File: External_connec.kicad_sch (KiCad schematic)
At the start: 12 parts, among them CN1 JST_Battery, J10 Conn_01x16_Socket, J2 A - B, J3 H - L, J4 TYPE-C-31-M12_13, J5 EXT_LOAD, J6 R4_TX, J7 R4_RX, J9 Conn_01x16_Socket

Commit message: Corrected schematic to PCB export error and warings and IP5306 and SD card section
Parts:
- CN1: footprint ESP32-S3_Dev_Board:CONN-SMD_2P-P1.00_SM02B-SRSS-TB-LF-SN -> ESP32-S3_Dev_Board:JST_2mm; LCSC Part C160402 -> C295747; PN SM02B-SRSS-TB (LF)(SN) -> S2B-PH-SM4-TB(LF)(SN)
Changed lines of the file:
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@@
       (effects (font (size 1.27 1.27)) hide)
     )
-    (property "Footprint" "ESP32-S3_Dev_Board:CONN-SMD_2P-P1.00_SM02B-SRSS-TB-LF-SN" (at 251.46 93.345 0)
+    (property "Footprint" "ESP32-S3_Dev_Board:JST_2mm" (at 251.46 93.345 0)
       (effects (font (size 1.27 1.27)) hide)
     )
-    (property "Datasheet" "https://lcsc.com/product-detail/Others_JST-Sales-America__JST-Sales-America-SM02B-SRSS-TB-LF-SN_C160402.html" (at 251.46 95.885 0)
+    (property "Datasheet" "https://datasheet.lcsc.com/lcsc/2102031704_JST-Sales-America-S2B-PH-SM4-TB-LF-SN_C295747.pdf" (at 251.46 95.885 0)
       (effects (font (size 1.27 1.27)) hide)
     )
-    (property "LCSC Part" "C160402" (at 251.46 98.425 0)
+    (property "LCSC Part" "C295747" (at 251.46 98.425 0)
       (effects (font (size 1.27 1.27)) hide)
     )
-    (property "PN" "SM02B-SRSS-TB (LF)(SN)" (at 251.46 89.535 0)
+    (property "PN" "S2B-PH-SM4-TB(LF)(SN) " (at 251.46 89.535 0)
       (effects (font (size 1.27 1.27)) hide)
     )

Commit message: Made minor changes in connectors sheet
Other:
- moved on the sheet: J10, J9

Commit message: Added CAN Jumpers, changed jumper pitch to 1.27mm
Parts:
- added J11: CAN_TX, ESP32-S3_Dev_Board:PinHeader_1x02_P1.27mm_Vertical, symbol ESP32-S3_DB:Conn_01x02
- added J12: CAN_RX, ESP32-S3_Dev_Board:PinHeader_1x02_P1.27mm_Vertical, symbol ESP32-S3_DB:Conn_01x02
- J6, J7: footprint ESP32-S3_Dev_Board:PinHeader_1x02_P2.54mm_Vertical -> ESP32-S3_Dev_Board:PinHeader_1x02_P1.27mm_Vertical
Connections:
- net CAN_RX renamed CAN_RX/GPIO8
- net CAN_RX/GPIO8: now also J12.1 (Pin_1)
- net CAN_TX renamed CAN_TX/GPIO7
- net CAN_TX/GPIO7: now also J11.1 (Pin_1)
- net RS-485_RX renamed RS-485_RX/GPIO46
- net RS-485_TX renamed RS-485_TX/GPIO45
- new net CAN_TRANS_RXD: J12.2 (Pin_2)
- new net CAN_TRANS_TXD: J11.2 (Pin_2)
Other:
- moved on the sheet: CN1

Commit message: Changed GPIO headers to Arduino style
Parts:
- removed J10, J9: Conn_01x16_Socket, ESP32-S3_Dev_Board:PinHeader_2x08_P2.54mm_Vertical, symbol ESP32-S3_DB:Conn_01x16_Socket
- added J13, J16: Conn_01x08, ESP32-S3_Dev_Board:PinHeader_1x08_P2.54mm_Vertical, symbol ESP32-S3_DB:Conn_01x08
- added J14, J9: Conn_01x06, ESP32-S3_Dev_Board:PinHeader_1x06_P2.54mm_Vertical, symbol ESP32-S3_DB:Conn_01x06
- added J15: Conn_01x10, ESP32-S3_Dev_Board:PinHeader_1x10_P2.54mm_Vertical, symbol ESP32-S3_DB:Conn_01x10
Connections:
- net 3V3: now also J16.5 (Pin_5), J9.6 (Pin_6)
- net 5V: now also J16.4 (Pin_4)
- net CAN_RX/GPIO8: now also J13.7 (Pin_7)
- net CAN_TX/GPIO7: now also J13.8 (Pin_8)
- net GND: now also J15.7 (Pin_7), J16.2 (Pin_2), J16.3 (Pin_3)
- net GPIO1: now also J14.1 (Pin_1)
- net GPIO14: now also J15.2 (Pin_2)
- net GPIO15: now also J15.3 (Pin_3)
- net GPIO16: now also J15.4 (Pin_4)
- net GPIO17: now also J15.5 (Pin_5)
- net GPIO18: now also J15.6 (Pin_6)
- net GPIO2: now also J14.2 (Pin_2)
- net GPIO21: now also J13.1 (Pin_1)
- net GPIO3: now also J14.3 (Pin_3)
- net GPIO33: now also J13.2 (Pin_2)
- net GPIO34: now also J13.3 (Pin_3)
- net GPIO35: now also J13.4 (Pin_4)
- net GPIO36: now also J13.5 (Pin_5)
- net GPIO37: now also J13.6 (Pin_6)
- net GPIO38: now also J15.9 (Pin_9)
- net GPIO39: now also J15.10 (Pin_10)
- net GPIO4: now also J14.4 (Pin_4)
- net GPIO40: now also J9.3 (Pin_3)
- net GPIO41: now also J9.4 (Pin_4)
- net GPIO42/~{RE}_DE: now also J9.5 (Pin_5)
- net GPIO5: now also J14.5 (Pin_5)
- net GPIO6: now also J14.6 (Pin_6)
- net GPIO9: now also J15.1 (Pin_1)
- net RS-485_RX/GPIO46: now also J9.2 (Pin_2)
- net RS-485_TX/GPIO45: now also J9.1 (Pin_1)
- new net RESET: J16.6 (Pin_6)
- no-connect marks 6 -> 10
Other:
- note added: "ADC GPIOs"
- note added: "DIGITAL GPIOs"
- note added: "JUMPER FOR USING CAN"
- note added: "POWER GPIOs"
- moved on the sheet: CN1, D11, J11, J12, J2, J3, J4, J5, J6, J7, R6, R7

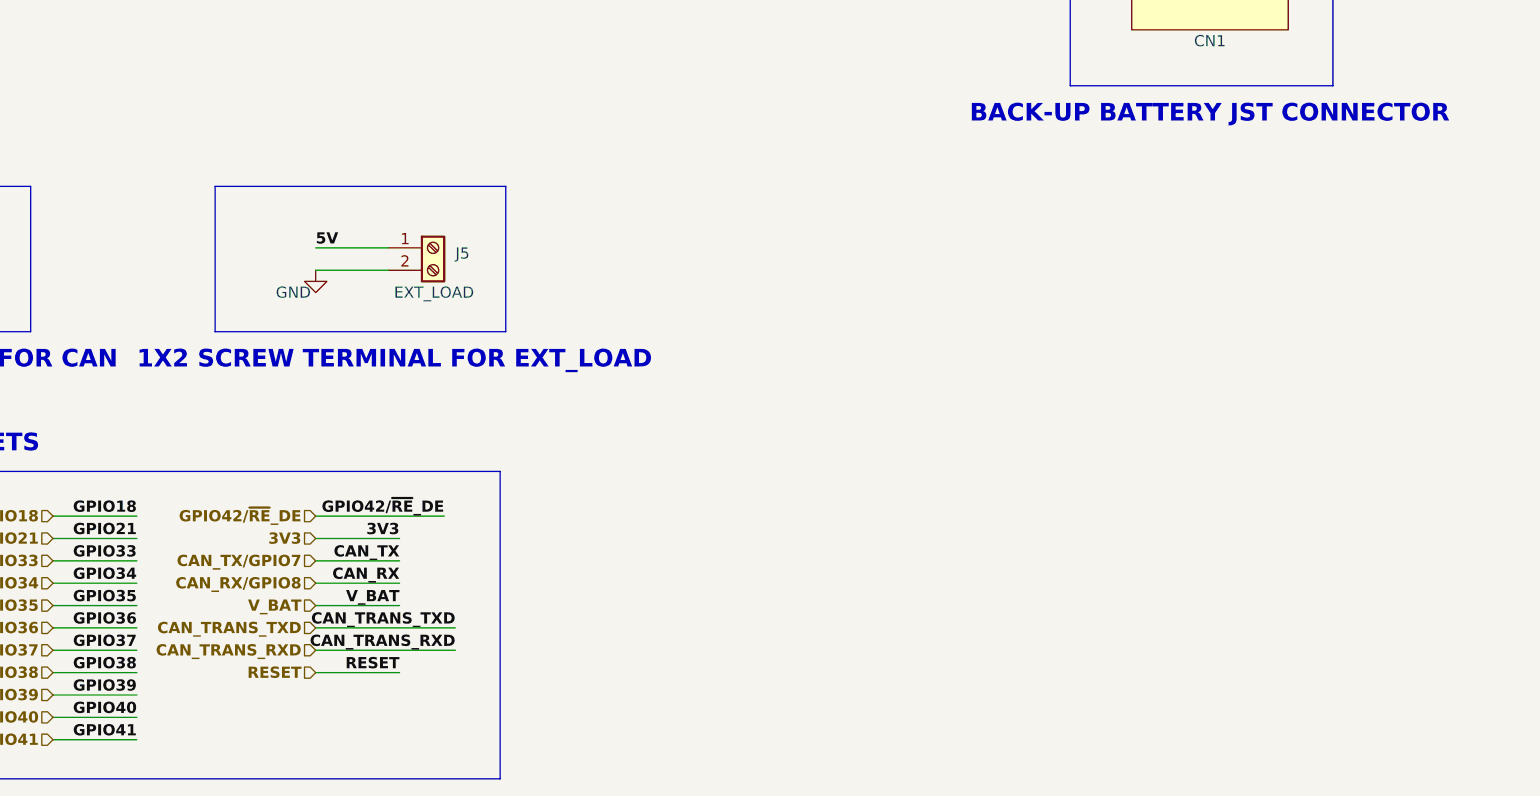
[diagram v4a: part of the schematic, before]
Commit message: Arranged IP5306, Added support for USB-To-RS485
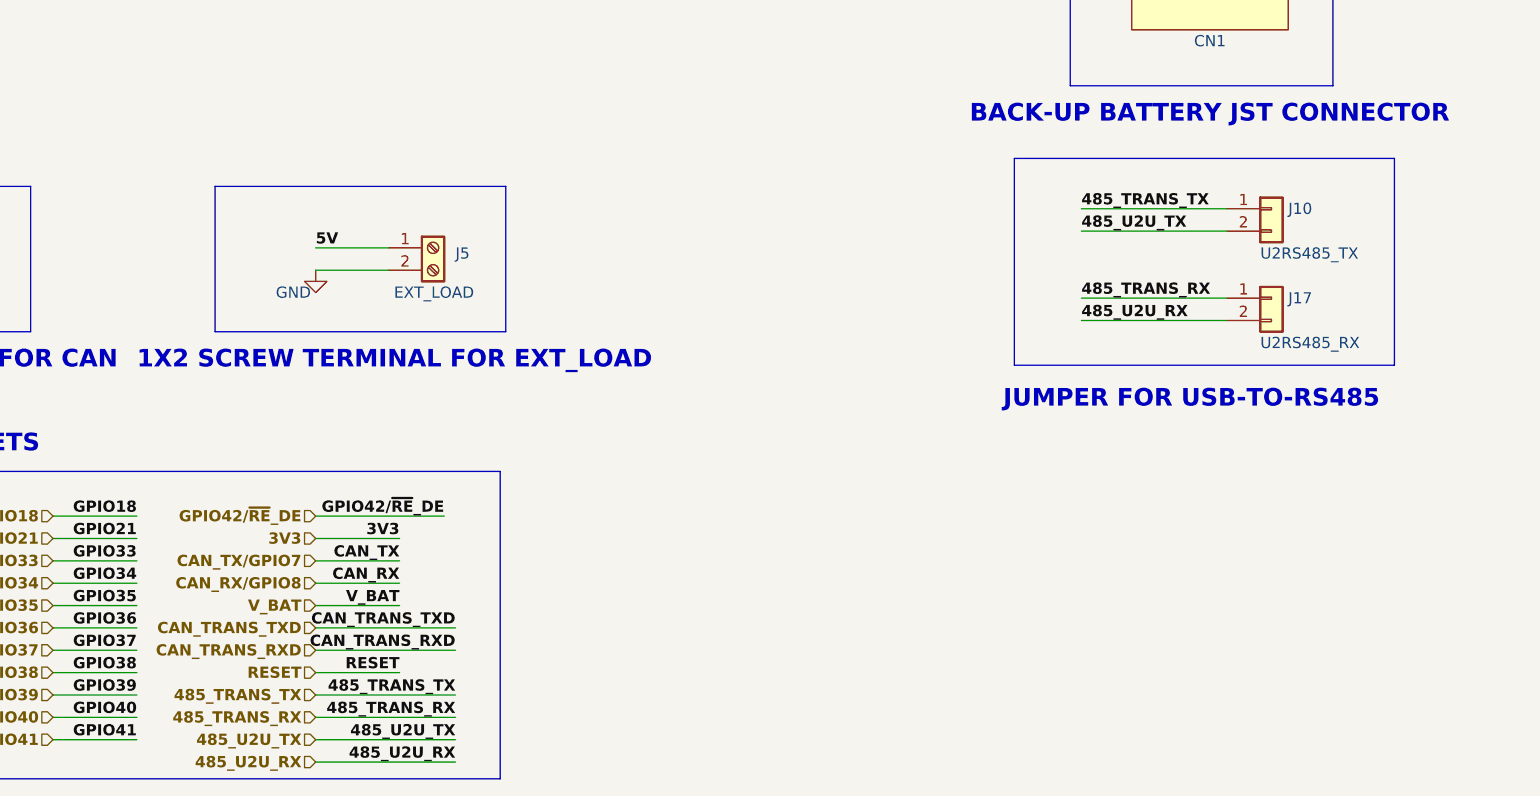
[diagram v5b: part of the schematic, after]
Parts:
- added J10: U2RS485_TX, ESP32-S3_Dev_Board:PinHeader_1x02_P1.27mm_Vertical, symbol ESP32-S3_DB:Conn_01x02
- added J17: U2RS485_RX, ESP32-S3_Dev_Board:PinHeader_1x02_P1.27mm_Vertical, symbol ESP32-S3_DB:Conn_01x02
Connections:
- new net 485_TRANS_RX: J17.1 (Pin_1)
- new net 485_TRANS_TX: J10.1 (Pin_1)
- new net 485_U2U_RX: J17.2 (Pin_2)
- new net 485_U2U_TX: J10.2 (Pin_2)
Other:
- note added: "JUMPER FOR USB-TO-RS485"

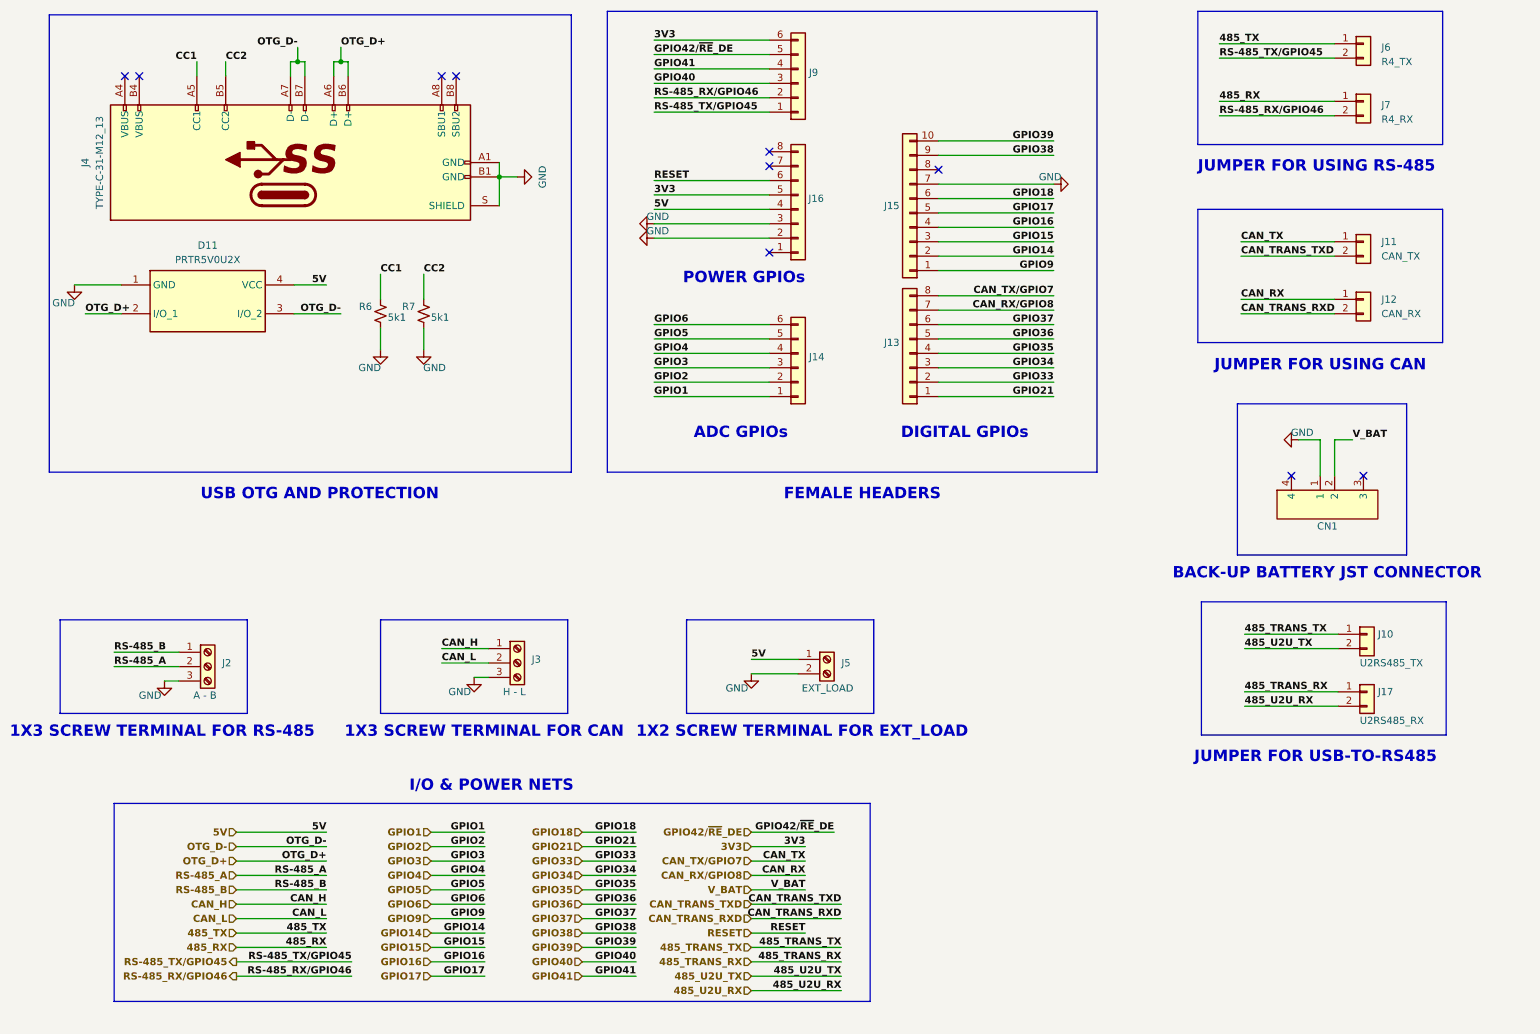
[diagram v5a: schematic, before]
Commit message: Added selection jumper sheet and USB-UART option for board
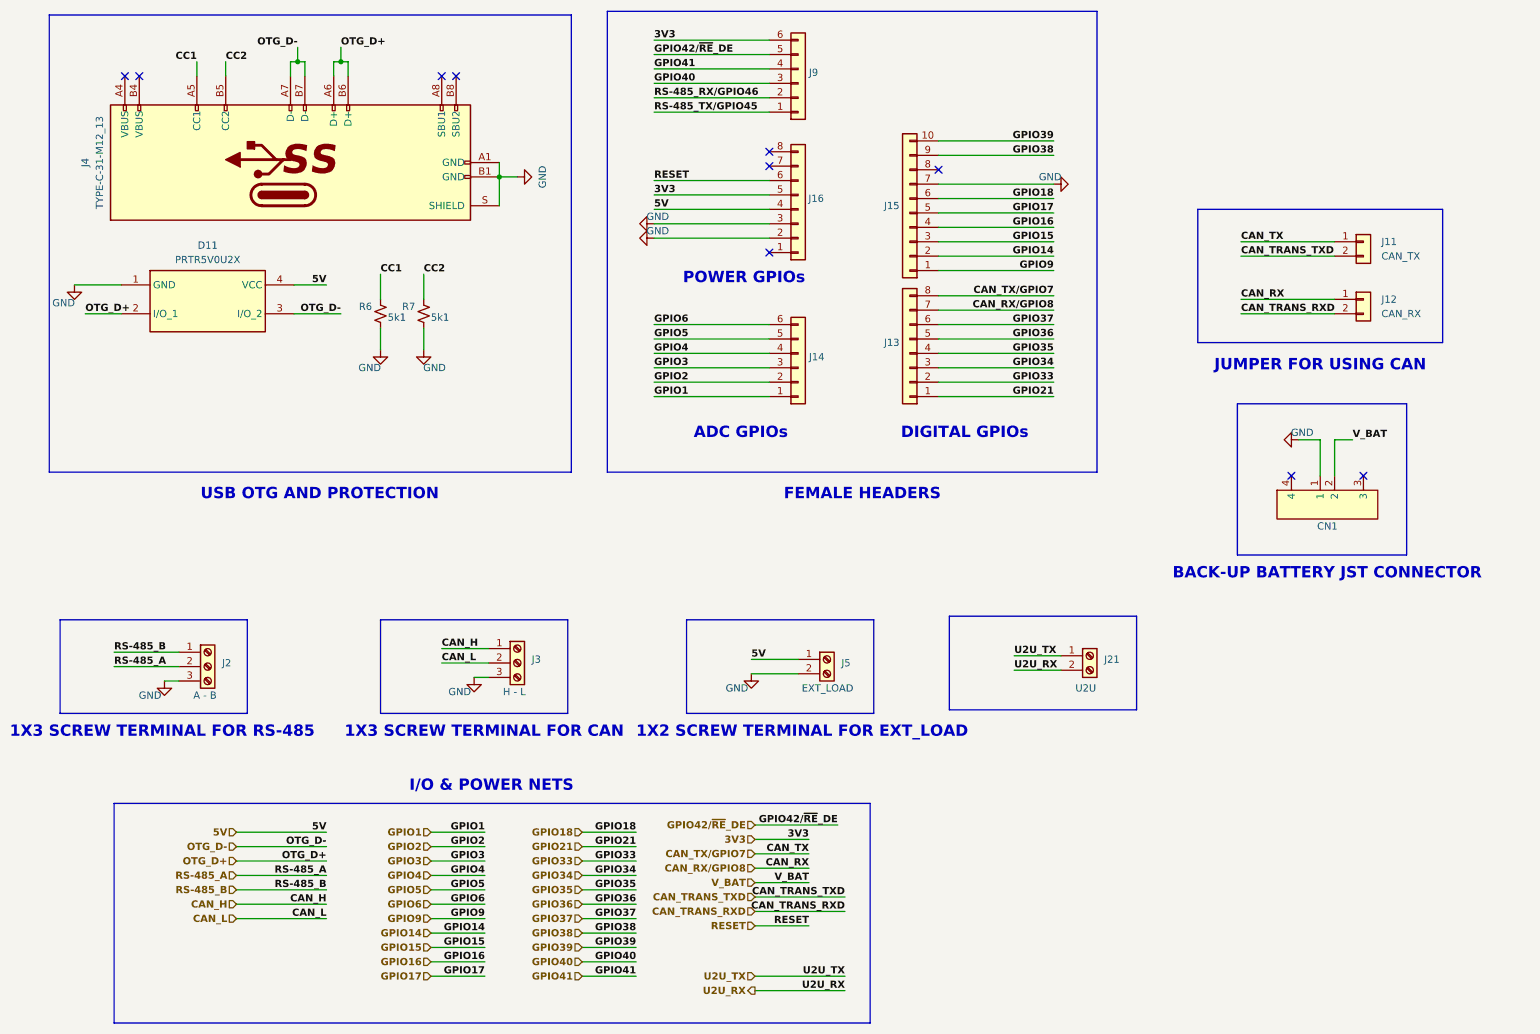
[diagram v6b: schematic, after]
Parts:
- removed J10: U2RS485_TX, ESP32-S3_Dev_Board:PinHeader_1x02_P1.27mm_Vertical, symbol ESP32-S3_DB:Conn_01x02
- removed J17: U2RS485_RX, ESP32-S3_Dev_Board:PinHeader_1x02_P1.27mm_Vertical, symbol ESP32-S3_DB:Conn_01x02
- removed J6: R4_TX, ESP32-S3_Dev_Board:PinHeader_1x02_P1.27mm_Vertical, symbol ESP32-S3_DB:Conn_01x02
- removed J7: R4_RX, ESP32-S3_Dev_Board:PinHeader_1x02_P1.27mm_Vertical, symbol ESP32-S3_DB:Conn_01x02
- added J21: U2U, ESP32-S3_Dev_Board:2P_Screw_Terminal, symbol ESP32-S3_DB:Screw_Terminal_01x02
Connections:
- new net U2U_RX: J21.2 (Pin_2)
- new net U2U_TX: J21.1 (Pin_1)
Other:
- note removed: "JUMPER FOR USB-TO-RS485"
- note removed: "JUMPER FOR USING RS-485"

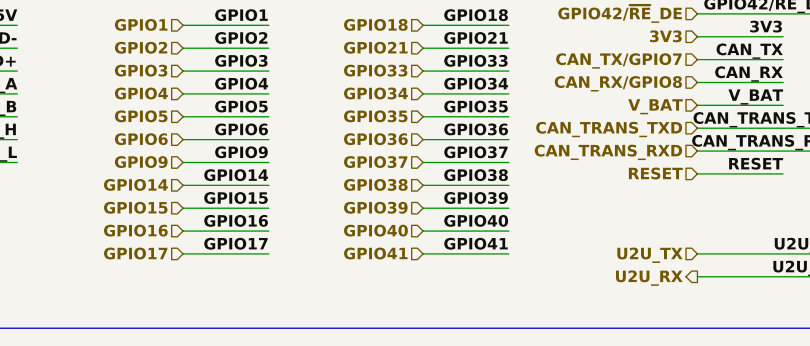
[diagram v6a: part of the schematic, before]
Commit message: Added mounting holes
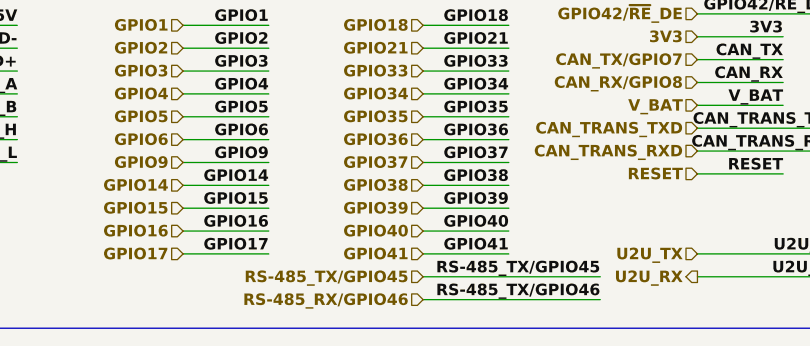
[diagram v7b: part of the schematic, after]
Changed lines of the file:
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@@
     (stroke (width 0.5) (type default) (color 132 132 0 1))
+  )
+  (wire (pts (xy 133.985 191.77) (xy 114.3 191.77))
+    (stroke (width 0.5) (type default) (color 0 0 255 1))
   )
   (wire (pts (xy 69.215 166.37) (xy 53.34 166.37))
@@
     (stroke (width 0.5) (type default) (color 0 0 0 1))
   )
+  (wire (pts (xy 133.985 189.23) (xy 114.3 189.23))
+    (stroke (width 0.5) (type default) (color 0 0 255 1))
+  )
   (wire (pts (xy 177.165 46.99) (xy 197.485 46.99))
     (stroke (width 0) (type default))
@@
     (effects (font (size 1.27 1.27) bold (color 72 0 0 1)) (justify right bottom))
   )
+  (label "RS-485_TX{slash}GPIO45" (at 133.985 189.23 180) (fields_autoplaced)
+    (effects (font (size 1.27 1.27) bold (color 0 0 255 1)) (justify right bottom))
+  )
   (label "GPIO39" (at 123.825 181.61 180) (fields_autoplaced)
     (effects (font (size 1.27 1.27) bold (color 72 0 0 1)) (justify right bottom))
@@
     (effects (font (size 1.27 1.27) bold (color 72 0 0 1)) (justify right bottom))
   )
+  (label "RS-485_TX{slash}GPIO46" (at 133.985 191.77 180) (fields_autoplaced)
+    (effects (font (size 1.27 1.27) bold (color 0 0 255 1)) (justify right bottom))
+  )
   (label "CAN_RX" (at 154.305 167.64 180) (fields_autoplaced)
     (effects (font (size 1.27 1.27) bold (color 0 0 255 1)) (justify right bottom))
@@
     (effects (font (size 1.27 1.27) (thickness 0.254) bold (color 72 0 72 1)) (justify right))
   )
+  (hierarchical_label "RS-485_RX{slash}GPIO46" (shape input) (at 114.3 191.77 180) (fields_autoplaced)
+    (effects (font (size 1.27 1.27) (thickness 0.254) bold (color 0 0 255 1)) (justify right))
+  )
+  (hierarchical_label "RS-485_TX{slash}GPIO45" (shape input) (at 114.3 189.23 180) (fields_autoplaced)
+    (effects (font (size 1.27 1.27) (thickness 0.254) bold (color 0 0 255 1)) (justify right))
+  )
   (hierarchical_label "GPIO2" (shape input) (at 87.63 163.83 180) (fields_autoplaced)
